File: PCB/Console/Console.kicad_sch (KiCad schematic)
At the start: 21 parts, among them J1 Conn_01x04_Socket, J1A1 Conn_01x04_Pin, J2 Conn_01x02_Socket, J2A1 Conn_01x02_Pin, J3 Conn_01x08_Socket, J3A1 Conn_01x08_Pin, J4 AC Plug, J5 DIN-6, J6 Conn_01x06_Socket, J6A1 Conn_01x06_Pin, J7 DIN-6, K1 Dual Relay Module, SW1 RotaryEncoder_Switch_MP, SW2 Pwr Switch, U1 WeMos D1 Mini32, U2 JXI 1.28in Round LCD

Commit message: Console: strip to console-side, GX16-6 connector, ERC clean
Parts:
- removed J4: AC Plug, symbol JK_And_Sons:AC_Plug
- removed J5, J7: DIN-6, symbol Connector:DIN-6
- removed J6: Conn_01x06_Socket, symbol Connector:Conn_01x06_Socket
- removed J6A1: Conn_01x06_Pin, symbol Connector:Conn_01x06_Pin
- removed K1: Dual Relay Module, symbol JK_And_Sons:Dual_Relay_Mod
- removed PS1: HS-40005, Converter_ACDC:Converter_ACDC_Hahn_HS-400xx_THT, symbol Converter_ACDC:HS-40005
- added J4: Conn_01x06, symbol Connector_Generic:Conn_01x06
- SW1: footprint (none) -> Rotary_Encoder:RotaryEncoder_Alps_EC12E-Switch_Vertical_H20mm
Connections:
- net 5Vdc: now also J4.1 (Pin_1)
- net Alarm: now also J4.6 (Pin_6)
- net GND: now also J4.2 (Pin_2), J4.4 (Pin_4)
- net Vac_Pump: now also J4.5 (Pin_5)
- net Vac_Sensor: now also J4.3 (Pin_3)
- net 5Vdc_Switched renamed 5Vdc_switched
- no-connect marks 22 -> 20
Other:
- note removed: "Low Voltage Signals"

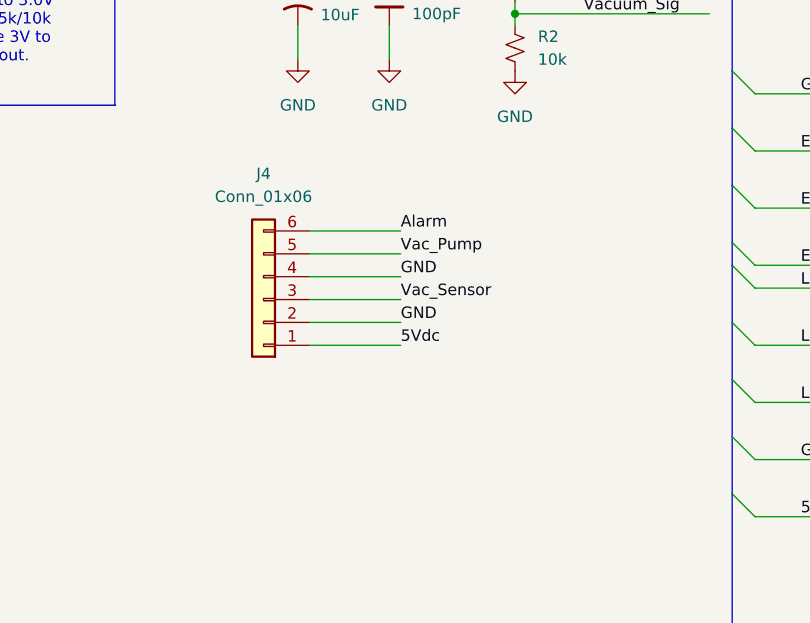
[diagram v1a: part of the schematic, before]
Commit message: Console: assign footprints (D1 Mini32 + JST XH + passives), verified pin mapping via F8
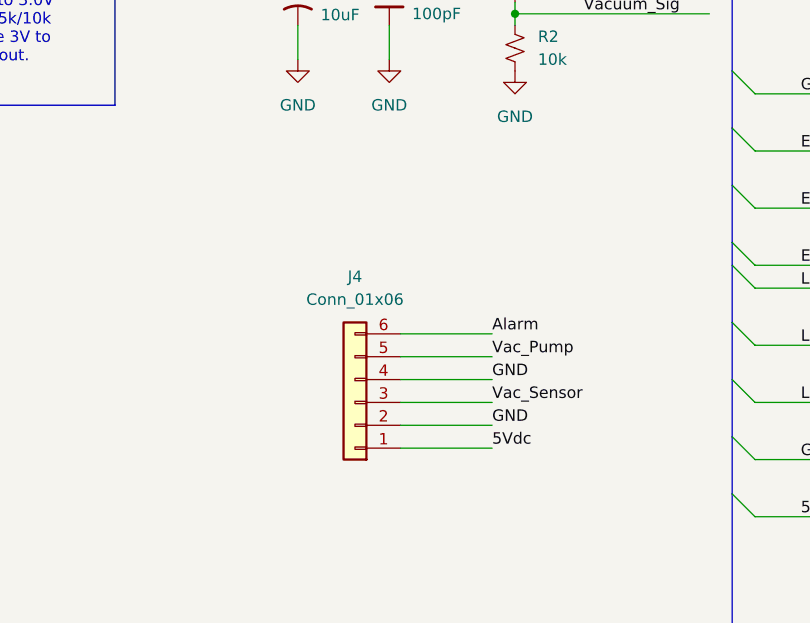
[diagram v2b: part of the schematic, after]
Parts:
- C1: footprint (none) -> Capacitor_THT:C_Radial_D8.0mm_H11.5mm_P3.50mm
- C3: footprint (none) -> Capacitor_THT:C_Disc_D3.8mm_W2.6mm_P2.50mm
- J1: footprint (none) -> Connector_JST:JST_XH_B4B-XH-A_1x04_P2.50mm_Vertical
- J2: footprint (none) -> Connector_JST:JST_XH_B2B-XH-A_1x02_P2.50mm_Vertical
- J3: footprint (none) -> Connector_JST:JST_XH_B8B-XH-A_1x08_P2.50mm_Vertical
- J4: footprint (none) -> Connector_JST:JST_XH_B6B-XH-A_1x06_P2.50mm_Vertical
- R1, R2: footprint (none) -> Resistor_THT:R_Axial_DIN0207_L6.3mm_D2.5mm_P7.62mm_Horizontal
- U1: footprint (none) -> ESP32_mini:ESP32_mini
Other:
- moved on the sheet: J4
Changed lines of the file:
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@@
 	(wire
 		(pts
-			(xy 66.04 67.31) (xy 76.2 67.31)
+			(xy 76.2 78.74) (xy 86.36 78.74)
 		)
 		(stroke
@@
 	(wire
 		(pts
-			(xy 66.04 64.77) (xy 76.2 64.77)
+			(xy 76.2 76.2) (xy 86.36 76.2)
 		)
 		(stroke
@@
 	(wire
 		(pts
-			(xy 66.04 62.23) (xy 76.2 62.23)
+			(xy 76.2 73.66) (xy 86.36 73.66)
 		)
 		(stroke
@@
 	(wire
 		(pts
-			(xy 66.04 69.85) (xy 76.2 69.85)
+			(xy 76.2 81.28) (xy 86.36 81.28)
 		)
 		(stroke
@@
 	(wire
 		(pts
-			(xy 66.04 59.69) (xy 76.2 59.69)
+			(xy 76.2 71.12) (xy 86.36 71.12)
 		)
 		(stroke
@@
 	(wire
 		(pts
-			(xy 66.04 57.15) (xy 76.2 57.15)
+			(xy 76.2 68.58) (xy 86.36 68.58)
 		)
 		(stroke
@@
 	)
 	(label "5Vdc"
-		(at 76.2 69.85 0)
+		(at 86.36 81.28 0)
 		(effects
 			(font
@@
 	)
 	(label "GND"
-		(at 76.2 67.31 0)
+		(at 86.36 78.74 0)
 		(effects
 			(font
@@
 	)
 	(label "Alarm"
-		(at 76.2 57.15 0)
+		(at 86.36 68.58 0)
 		(effects
 			(font
@@
 	)
 	(label "GND"
-		(at 76.2 62.23 0)
+		(at 86.36 73.66 0)
 		(effects
 			(font
@@
 	)
 	(label "Vac_Pump"
-		(at 76.2 59.69 0)
+		(at 86.36 71.12 0)
 		(effects
 			(font
@@
 	)
 	(label "Vac_Sensor"
-		(at 76.2 64.77 0)
+		(at 86.36 76.2 0)
 		(effects
 			(font
@@
 			)
 		)
-		(property "Footprint" ""
+		(property "Footprint" "Capacitor_THT:C_Radial_D8.0mm_H11.5mm_P3.50mm"
 			(at 64.77 31.75 0)
 			(hide yes)
@@
 			)
 		)
-		(property "Footprint" ""
+		(property "Footprint" "Resistor_THT:R_Axial_DIN0207_L6.3mm_D2.5mm_P7.62mm_Horizontal"
 			(at 88.9 29.21 0)
 			(hide yes)
@@
 		(exclude_from_sim no)
 		(in_bom yes)
-		(on_board yes)
+		(on_board no)
 		(in_pos_files yes)
 		(dnp no)
@@
 			)
 		)
-		(property "Footprint" ""
+		(property "Footprint" "Capacitor_THT:C_Disc_D3.8mm_W2.6mm_P2.50mm"
 			(at 74.93 31.75 0)
 			(hide yes)
@@
 			)
 		)
-		(property "Footprint" ""
+		(property "Footprint" "Connector_JST:JST_XH_B8B-XH-A_1x08_P2.50mm_Vertical"
 			(at 215.9 105.41 0)
 			(hide yes)
@@
 		(exclude_from_sim no)
 		(in_bom yes)
-		(on_board yes)
+		(on_board no)
 		(in_pos_files yes)
 		(dnp no)
@@
 			)
 		)
-		(property "Footprint" ""
+		(property "Footprint" "ESP32_mini:ESP32_mini"
 			(at 139.7 39.37 0)
 			(hide yes)
@@
 		(exclude_from_sim no)
 		(in_bom yes)
-		(on_board yes)
+		(on_board no)
 		(in_pos_files yes)
 		(dnp no)
@@
 		(exclude_from_sim no)
 		(in_bom yes)
-		(on_board yes)
+		(on_board no)
 		(in_pos_files yes)
 		(dnp no)
@@
 			)
 		)
-		(property "Footprint" ""
+		(property "Footprint" "Resistor_THT:R_Axial_DIN0207_L6.3mm_D2.5mm_P7.62mm_Horizontal"
 			(at 88.9 36.83 0)
 			(hide yes)
@@
 		(exclude_from_sim no)
 		(in_bom yes)
-		(on_board yes)
+		(on_board no)
 		(in_pos_files yes)
 		(dnp no)
@@
 		(exclude_from_sim no)
 		(in_bom yes)
-		(on_board yes)
+		(on_board no)
 		(in_pos_files yes)
 		(dnp no)
@@
 			)
 		)
-		(property "Footprint" ""
+		(property "Footprint" "Connector_JST:JST_XH_B4B-XH-A_1x04_P2.50mm_Vertical"
 			(at 215.9 60.96 0)
 			(hide yes)
@@
 			)
 		)
-		(property "Footprint" ""
+		(property "Footprint" "Connector_JST:JST_XH_B2B-XH-A_1x02_P2.50mm_Vertical"
 			(at 217.17 33.02 0)
 			(hide yes)
@@
 	(symbol
 		(lib_id "Connector_Generic:Conn_01x06")
-		(at 60.96 64.77 180)
+		(at 71.12 76.2 180)
 		(unit 1)
 		(body_style 1)
@@
 		(fields_autoplaced yes)
 		(property "Reference" "J4"
-			(at 60.96 50.8 0)
+			(at 71.12 62.23 0)
 			(show_name no)
 			(do_not_autoplace no)
@@
 		)
 		(property "Value" "Conn_01x06"
-			(at 60.96 53.34 0)
+			(at 71.12 64.77 0)
 			(show_name no)
 			(do_not_autoplace no)
@@
 			)
 		)
-		(property "Footprint" ""
-			(at 60.96 64.77 0)
+		(property "Footprint" "Connector_JST:JST_XH_B6B-XH-A_1x06_P2.50mm_Vertical"
+			(at 71.12 76.2 0)
 			(hide yes)
 			(show_name no)
@@
 		)
 		(property "Datasheet" ""
-			(at 60.96 64.77 0)
+			(at 71.12 76.2 0)
 			(hide yes)
 			(show_name no)
@@
 		)
 		(property "Description" "Generic connector, single row, 01x06, script generated (kicad-library-utils/schlib/autogen/connector/)"
-			(at 60.96 64.77 0)
+			(at 71.12 76.2 0)
 			(hide yes)
 			(show_name no)

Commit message: Console: swap Waveshare pigtail for M128 7-pin socket (J3); F8 to PCB
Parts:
- removed J1: Conn_01x04_Socket, Connector_JST:JST_XH_B4B-XH-A_1x04_P2.50mm_Vertical, symbol Connector:Conn_01x04_Socket
- removed J1A1: Conn_01x04_Pin, symbol Connector:Conn_01x04_Pin
- removed J3: Conn_01x08_Socket, Connector_JST:JST_XH_B8B-XH-A_1x08_P2.50mm_Vertical, symbol Connector:Conn_01x08_Socket
- removed J3A1: Conn_01x08_Pin, symbol Connector:Conn_01x08_Pin
- removed U2: JXI 1.28in Round LCD, symbol JK_And_Sons:JXI_1pt28in_LCD
- added J3: Conn_01x07, Connector_PinSocket_2.54mm:PinSocket_1x07_P2.54mm_Vertical, symbol Connector_Generic:Conn_01x07
- SW1: footprint Rotary_Encoder:RotaryEncoder_Alps_EC12E-Switch_Vertical_H20mm -> Rotary_Encoder:RotaryEncoder_Alps_EC11E-Switch_Vertical_H20mm
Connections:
- net GND: now also J3.2 (Pin_2)
- net LCD_CS: now also J3.6 (Pin_6)
- net LCD_DC: now also J3.5 (Pin_5)
- net LCD_MOSI: now also J3.4 (Pin_4)
- net LCD_RST: now also J3.7 (Pin_7)
- net LCD_SClk: now also J3.3 (Pin_3)
- net LCD_Vcc: now also J3.1 (Pin_1)
- net LCD_BackLt: no longer names the net of U1.8 (IO21)
- net LCD_MISO: no longer names the net of U1.29 (IO19)
- no-connect marks 20 -> 22
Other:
- note removed: "Blk"
- note removed: "Blu"
- note removed: "Grn"
- note removed: "Org"
- note removed: "Pur"
- note removed: "Red"
- note removed: "Wht"
- note removed: "Yel"
